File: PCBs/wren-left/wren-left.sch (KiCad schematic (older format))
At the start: 95 parts, among them J1 TRRS_Jack, SW0 Reset, U1 Elite-C

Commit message: Reposition Rotary Encoder and Create New Right Board
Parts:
- added H1, H2, H3, H4, H5, H6, H7: MountingHole, MountingHole:MountingHole_2.2mm_M2_ISO7380, symbol Mechanical:MountingHole
- U1: symbol keebio:Elite-C -> wren-left-rescue:Elite-C-keebio
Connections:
- net COL0: now also MX41.1 (COL); no longer ENC1.S1
- net COL1: now also MX42.1 (COL); no longer MX41.1 (COL)
- net COL2: now also MX43.1 (COL); no longer MX42.1 (COL)
- net COL3: now also MX44.1 (COL); no longer MX43.1 (COL)
- net COL4: now also ENC1.S2; no longer MX44.1 (COL)
- net at MX41.2 (ROW): now also D41.2 (A); no longer D42.2 (A)
- net at MX42.2 (ROW): now also D42.2 (A); no longer D43.2 (A)
- net at MX43.2 (ROW): now also D43.2 (A); no longer D44.2 (A)
- net at MX44.2 (ROW): now also D44.2 (A); no longer D45.2 (A)
- removed net ENC1-OUT: D41.2 (A), ENC1.S2
- new net ENC1-IN: D45.2 (A), ENC1.S1
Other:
- moved on the sheet: ENC1, MX41, MX42, MX43, MX44
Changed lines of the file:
@@
 $EndComp
 $Comp
-L MX_Alps_Hybrid:MX-NoLED MX41
-U 1 1 6072AAD1
+L MX_Alps_Hybrid:MX-NoLED MX42
+U 1 1 6072B58C
 P 5600 5550
-F 0 "MX41" H 5633 5773 60  0000 C CNN
+F 0 "MX42" H 5633 5773 60  0000 C CNN
 F 1 "MX-NoLED" H 5633 5699 20  0000 C CNN
-F 2 "MX_Only:MX-2U-FLIPPED-ReversedStabilizers" H 4975 5525 60  0001 C CNN
+F 2 "MX_Only:MX-1U" H 4975 5525 60  0001 C CNN
 F 3 "" H 4975 5525 60  0001 C CNN
 	1    5600 5550
@@
 $EndComp
 $Comp
-L MX_Alps_Hybrid:MX-NoLED MX42
-U 1 1 6072B58C
+L MX_Alps_Hybrid:MX-NoLED MX43
+U 1 1 6072BC7D
 P 6100 5550
-F 0 "MX42" H 6133 5773 60  0000 C CNN
+F 0 "MX43" H 6133 5773 60  0000 C CNN
 F 1 "MX-NoLED" H 6133 5699 20  0000 C CNN
 F 2 "MX_Only:MX-1U" H 5475 5525 60  0001 C CNN
@@
 $EndComp
 $Comp
-L MX_Alps_Hybrid:MX-NoLED MX43
-U 1 1 6072BC7D
+L MX_Alps_Hybrid:MX-NoLED MX44
+U 1 1 6072C094
 P 6600 5550
-F 0 "MX43" H 6633 5773 60  0000 C CNN
+F 0 "MX44" H 6633 5773 60  0000 C CNN
 F 1 "MX-NoLED" H 6633 5699 20  0000 C CNN
 F 2 "MX_Only:MX-1U" H 5975 5525 60  0001 C CNN
 F 3 "" H 5975 5525 60  0001 C CNN
 	1    6600 5550
-	1    0    0    -1
-$EndComp
-$Comp
-L MX_Alps_Hybrid:MX-NoLED MX44
-U 1 1 6072C094
-P 7100 5550
-F 0 "MX44" H 7133 5773 60  0000 C CNN
-F 1 "MX-NoLED" H 7133 5699 20  0000 C CNN
-F 2 "MX_Only:MX-1U" H 6475 5525 60  0001 C CNN
-F 3 "" H 6475 5525 60  0001 C CNN
-	1    7100 5550
 	1    0    0    -1
 $EndComp
@@
 L Device:Rotary_Encoder_Switch ENC1
 U 1 1 60759DC4
-P 1700 6350
-F 0 "ENC1" H 1700 6717 50  0000 C CNN
-F 1 "Rotary_Encoder_Switch" H 1700 6626 50  0000 C CNN
-F 2 "Rotary_Encoder:RotaryEncoder_Alps_EC11E-Switch_Vertical_H20mm" H 1550 6510 50  0001 C CNN
-F 3 "~" H 1700 6610 50  0001 C CNN
-	1    1700 6350
-	1    0    0    -1
-$EndComp
-Text GLabel 1400 6350 0    50   Input ~ 0
+P 2550 5700
+F 0 "ENC1" H 2550 6067 50  0000 C CNN
+F 1 "Rotary_Encoder_Switch" H 2550 5976 50  0000 C CNN
+F 2 "Rotary_Encoder:RotaryEncoder_Alps_EC11E-Switch_Vertical_H20mm" H 2400 5860 50  0001 C CNN
+F 3 "~" H 2550 5960 50  0001 C CNN
+	1    2550 5700
+	1    0    0    -1
+$EndComp
+Text GLabel 2250 5700 0    50   Input ~ 0
 GND
 Connection ~ 7250 4800
@@
 	5250 4800 5250 5500
 Connection ~ 5250 4800
+Connection ~ 4850 5900
+Wire Wire Line
+	4850 5900 5350 5900
+Text GLabel 2850 5600 2    50   Input ~ 0
+ENC1-IN
+Text GLabel 2850 5800 2    50   Input ~ 0
+ENC1-OUT
+Text GLabel 7050 5700 2    50   Input ~ 0
+ENC1-IN
+Text GLabel 2250 5600 0    50   Input ~ 0
+LEFT
+Text GLabel 2250 5800 0    50   Input ~ 0
+RIGHT
+$Comp
+L wren-left-rescue:Elite-C-keebio U1
+U 1 1 6071F7CA
+P 2500 2000
+F 0 "U1" H 2500 2815 50  0000 C CNN
+F 1 "Elite-C" H 2500 2724 50  0000 C CNN
+F 2 "footprints:Elite-C" H 2450 2100 50  0001 C CNN
+F 3 "" H 2450 2100 50  0001 C CNN
+	1    2500 2000
+	1    0    0    -1
+$EndComp
+Text GLabel 2700 2950 3    50   Input ~ 0
+LEFT
+Text GLabel 2600 2950 3    50   Input ~ 0
+RIGHT
+NoConn ~ 2300 2950
+NoConn ~ 2400 2950
+$Comp
+L MX_Alps_Hybrid:MX-NoLED MX41
+U 1 1 6072AAD1
+P 5100 5550
+F 0 "MX41" H 5133 5773 60  0000 C CNN
+F 1 "MX-NoLED" H 5133 5699 20  0000 C CNN
+F 2 "MX_Only:MX-2U-FLIPPED-ReversedStabilizers" H 4475 5525 60  0001 C CNN
+F 3 "" H 4475 5525 60  0001 C CNN
+	1    5100 5550
+	1    0    0    -1
+$EndComp
 $Comp
 L Device:D_Small D41
@@
 	0    -1   -1   0
 $EndComp
-Connection ~ 4850 5900
-Wire Wire Line
-	4850 5900 5350 5900
-Text GLabel 2000 6250 2    50   Input ~ 0
-ENC1-IN
-Text GLabel 2000 6450 2    50   Input ~ 0
+Text GLabel 7250 5500 0    50   Input ~ 0
 ENC1-OUT
-Text GLabel 4850 5700 0    50   Input ~ 0
-ENC1-OUT
-Text GLabel 5250 5500 0    50   Input ~ 0
-ENC1-IN
-Text GLabel 1400 6250 0    50   Input ~ 0
-LEFT
-Text GLabel 1400 6450 0    50   Input ~ 0
-RIGHT
-$Comp
-L keebio:Elite-C U1
-U 1 1 6071F7CA
-P 2500 2000
-F 0 "U1" H 2500 2815 50  0000 C CNN
-F 1 "Elite-C" H 2500 2724 50  0000 C CNN
-F 2 "footprints:Elite-C" H 2450 2100 50  0001 C CNN
-F 3 "" H 2450 2100 50  0001 C CNN
-	1    2500 2000
-	1    0    0    -1
-$EndComp
-Text GLabel 2700 2950 3    50   Input ~ 0
-LEFT
-Text GLabel 2600 2950 3    50   Input ~ 0
-RIGHT
-NoConn ~ 2300 2950
-NoConn ~ 2400 2950
+$Comp
+L Mechanical:MountingHole H3
+U 1 1 607DC9F0
+P 2500 7000
+F 0 "H3" H 2600 7046 50  0000 L CNN
+F 1 "MountingHole" H 2600 6955 50  0000 L CNN
+F 2 "MountingHole:MountingHole_2.2mm_M2_ISO7380" H 2500 7000 50  0001 C CNN
+F 3 "~" H 2500 7000 50  0001 C CNN
+	1    2500 7000
+	1    0    0    -1
+$EndComp
+$Comp
+L Mechanical:MountingHole H5
+U 1 1 607DDEC1
+P 2500 7200
+F 0 "H5" H 2600 7246 50  0000 L CNN
+F 1 "MountingHole" H 2600 7155 50  0000 L CNN
+F 2 "MountingHole:MountingHole_2.2mm_M2_ISO7380" H 2500 7200 50  0001 C CNN
+F 3 "~" H 2500 7200 50  0001 C CNN
+	1    2500 7200
+	1    0    0    -1
+$EndComp
+$Comp
+L Mechanical:MountingHole H7
+U 1 1 607DE302
+P 2500 7400
+F 0 "H7" H 2600 7446 50  0000 L CNN
+F 1 "MountingHole" H 2600 7355 50  0000 L CNN
+F 2 "MountingHole:MountingHole_2.2mm_M2_ISO7380" H 2500 7400 50  0001 C CNN
+F 3 "~" H 2500 7400 50  0001 C CNN
+	1    2500 7400
+	1    0    0    -1
+$EndComp
+$Comp
+L Mechanical:MountingHole H1
+U 1 1 607DE5EF
+P 2500 6800
+F 0 "H1" H 2600 6846 50  0000 L CNN
+F 1 "MountingHole" H 2600 6755 50  0000 L CNN
+F 2 "MountingHole:MountingHole_2.2mm_M2_ISO7380" H 2500 6800 50  0001 C CNN
+F 3 "~" H 2500 6800 50  0001 C CNN
+	1    2500 6800
+	1    0    0    -1
+$EndComp
+$Comp
+L Mechanical:MountingHole H2
+U 1 1 607DE9D9
+P 3250 6800
+F 0 "H2" H 3350 6846 50  0000 L CNN
+F 1 "MountingHole" H 3350 6755 50  0000 L CNN
+F 2 "MountingHole:MountingHole_2.2mm_M2_ISO7380" H 3250 6800 50  0001 C CNN
+F 3 "~" H 3250 6800 50  0001 C CNN
+	1    3250 6800
+	1    0    0    -1
+$EndComp
+$Comp
+L Mechanical:MountingHole H4
+U 1 1 607DED77
+P 3250 7000
+F 0 "H4" H 3350 7046 50  0000 L CNN
+F 1 "MountingHole" H 3350 6955 50  0000 L CNN
+F 2 "MountingHole:MountingHole_2.2mm_M2_ISO7380" H 3250 7000 50  0001 C CNN
+F 3 "~" H 3250 7000 50  0001 C CNN
+	1    3250 7000
+	1    0    0    -1
+$EndComp
+$Comp
+L Mechanical:MountingHole H6
+U 1 1 607DF460
+P 3250 7200
+F 0 "H6" H 3350 7246 50  0000 L CNN
+F 1 "MountingHole" H 3350 7155 50  0000 L CNN
+F 2 "MountingHole:MountingHole_2.2mm_M2_ISO7380" H 3250 7200 50  0001 C CNN
+F 3 "~" H 3250 7200 50  0001 C CNN
+	1    3250 7200
+	1    0    0    -1
+$EndComp
+Wire Wire Line
+	4850 5700 5050 5700
 $EndSCHEMATC

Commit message: Various Updates
New plates, updated routing on the right side, assorted other changes.
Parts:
- H1, H2, H3, H4, H5, H6, H7: footprint MountingHole:MountingHole_2.2mm_M2_ISO7380 -> MountingHole:MountingHole_5.5mm
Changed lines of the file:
@@
 F 0 "H3" H 2600 7046 50  0000 L CNN
 F 1 "MountingHole" H 2600 6955 50  0000 L CNN
-F 2 "MountingHole:MountingHole_2.2mm_M2_ISO7380" H 2500 7000 50  0001 C CNN
+F 2 "MountingHole:MountingHole_5.5mm" H 2500 7000 50  0001 C CNN
 F 3 "~" H 2500 7000 50  0001 C CNN
 	1    2500 7000
@@
 F 0 "H5" H 2600 7246 50  0000 L CNN
 F 1 "MountingHole" H 2600 7155 50  0000 L CNN
-F 2 "MountingHole:MountingHole_2.2mm_M2_ISO7380" H 2500 7200 50  0001 C CNN
+F 2 "MountingHole:MountingHole_5.5mm" H 2500 7200 50  0001 C CNN
 F 3 "~" H 2500 7200 50  0001 C CNN
 	1    2500 7200
@@
 F 0 "H7" H 2600 7446 50  0000 L CNN
 F 1 "MountingHole" H 2600 7355 50  0000 L CNN
-F 2 "MountingHole:MountingHole_2.2mm_M2_ISO7380" H 2500 7400 50  0001 C CNN
+F 2 "MountingHole:MountingHole_5.5mm" H 2500 7400 50  0001 C CNN
 F 3 "~" H 2500 7400 50  0001 C CNN
 	1    2500 7400
@@
 F 0 "H1" H 2600 6846 50  0000 L CNN
 F 1 "MountingHole" H 2600 6755 50  0000 L CNN
-F 2 "MountingHole:MountingHole_2.2mm_M2_ISO7380" H 2500 6800 50  0001 C CNN
+F 2 "MountingHole:MountingHole_5.5mm" H 2500 6800 50  0001 C CNN
 F 3 "~" H 2500 6800 50  0001 C CNN
 	1    2500 6800
@@
 F 0 "H2" H 3350 6846 50  0000 L CNN
 F 1 "MountingHole" H 3350 6755 50  0000 L CNN
-F 2 "MountingHole:MountingHole_2.2mm_M2_ISO7380" H 3250 6800 50  0001 C CNN
+F 2 "MountingHole:MountingHole_5.5mm" H 3250 6800 50  0001 C CNN
 F 3 "~" H 3250 6800 50  0001 C CNN
 	1    3250 6800
@@
 F 0 "H4" H 3350 7046 50  0000 L CNN
 F 1 "MountingHole" H 3350 6955 50  0000 L CNN
-F 2 "MountingHole:MountingHole_2.2mm_M2_ISO7380" H 3250 7000 50  0001 C CNN
+F 2 "MountingHole:MountingHole_5.5mm" H 3250 7000 50  0001 C CNN
 F 3 "~" H 3250 7000 50  0001 C CNN
 	1    3250 7000
@@
 F 0 "H6" H 3350 7246 50  0000 L CNN
 F 1 "MountingHole" H 3350 7155 50  0000 L CNN
-F 2 "MountingHole:MountingHole_2.2mm_M2_ISO7380" H 3250 7200 50  0001 C CNN
+F 2 "MountingHole:MountingHole_5.5mm" H 3250 7200 50  0001 C CNN
 F 3 "~" H 3250 7200 50  0001 C CNN
 	1    3250 7200

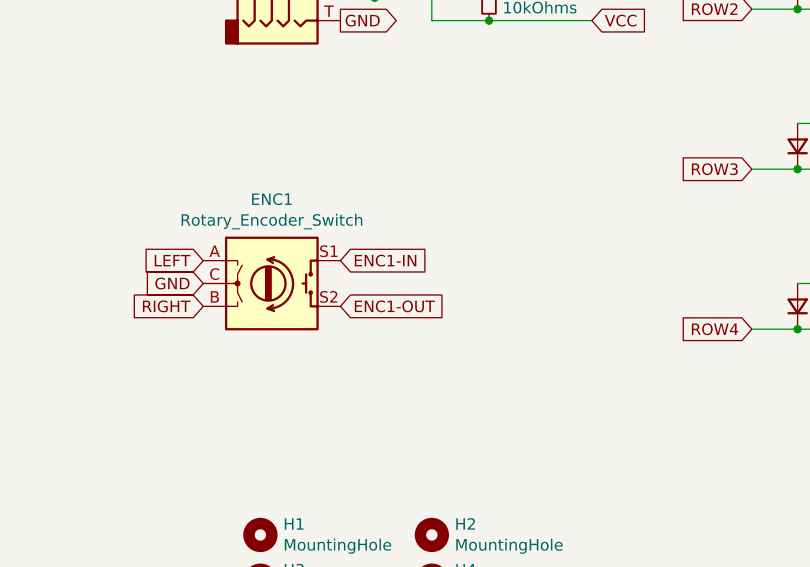
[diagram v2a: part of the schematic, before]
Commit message: Use insight on rotary encoder position to adopt more Kyria-like stagger
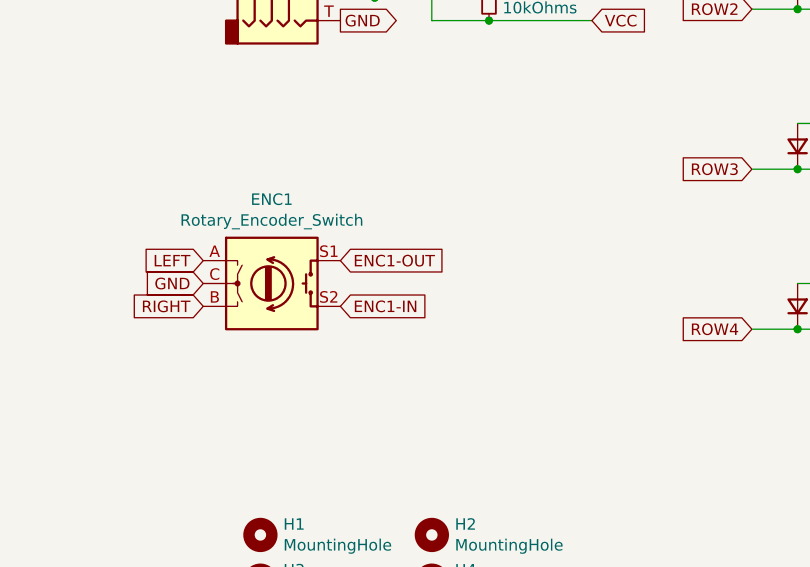
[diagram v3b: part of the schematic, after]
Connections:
- net COL4: now also ENC1.S1; no longer ENC1.S2
- net ENC1-IN: now also ENC1.S2; no longer ENC1.S1
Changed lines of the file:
@@
 Wire Wire Line
 	4850 5900 5350 5900
+Text GLabel 2850 5800 2    50   Input ~ 0
+ENC1-IN
 Text GLabel 2850 5600 2    50   Input ~ 0
-ENC1-IN
-Text GLabel 2850 5800 2    50   Input ~ 0
 ENC1-OUT
 Text GLabel 7050 5700 2    50   Input ~ 0

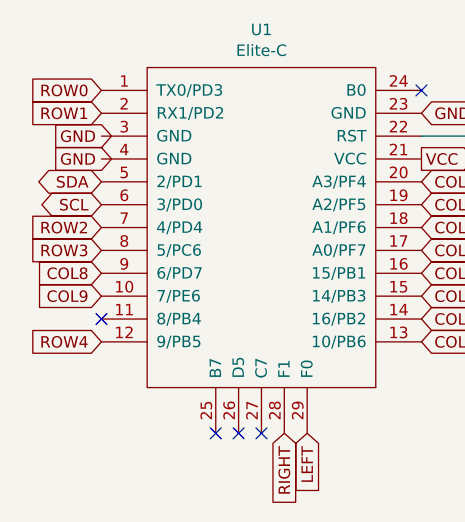
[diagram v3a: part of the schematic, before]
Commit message: Finish left side kyria-like stagger
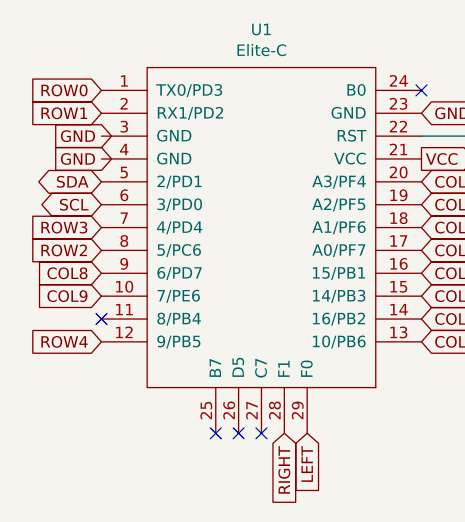
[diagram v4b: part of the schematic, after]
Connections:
- net ROW2: now also U1.8 (5/PC6); no longer U1.7 (4/PD4)
- net ROW3: now also U1.7 (4/PD4); no longer U1.8 (5/PC6)
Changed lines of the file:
@@
 Text GLabel 1800 1550 0    50   Input ~ 0
 ROW1
+Text GLabel 1800 2150 0    50   Input ~ 0
+ROW2
 Text GLabel 1800 2050 0    50   Input ~ 0
-ROW2
-Text GLabel 1800 2150 0    50   Input ~ 0
 ROW3
 Text GLabel 1800 2550 0    50   Input ~ 0

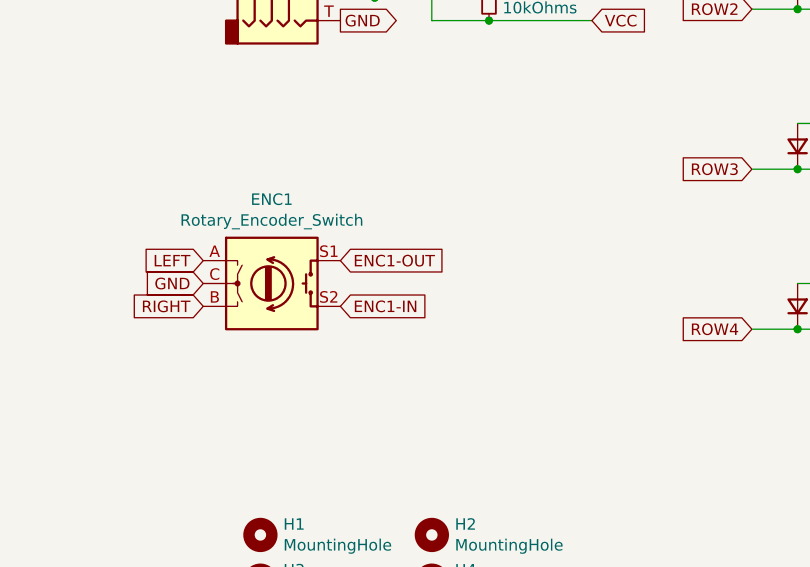
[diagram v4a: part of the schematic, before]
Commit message: Finalize encoder position on left side
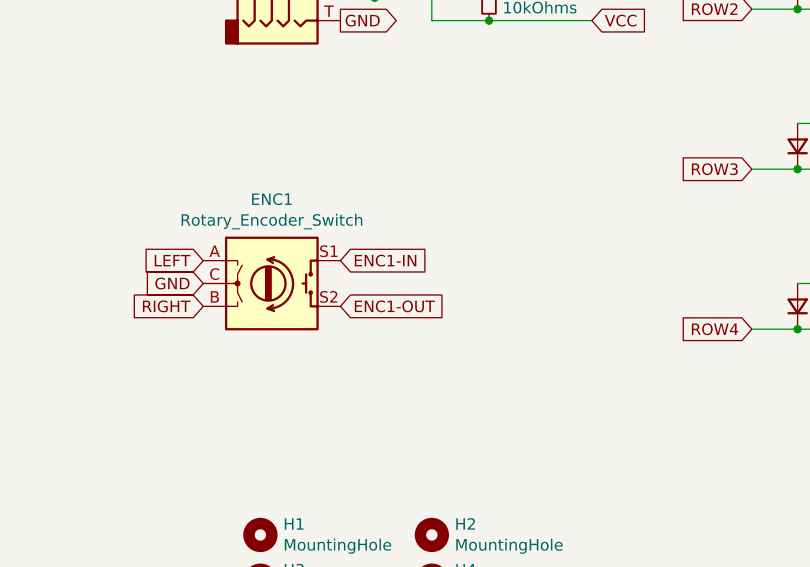
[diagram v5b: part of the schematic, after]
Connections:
- net COL4: now also ENC1.S2; no longer ENC1.S1
- net ENC1-IN: now also ENC1.S1; no longer ENC1.S2
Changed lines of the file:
@@
 Wire Wire Line
 	4850 5900 5350 5900
+Text GLabel 2850 5600 2    50   Input ~ 0
+ENC1-IN
 Text GLabel 2850 5800 2    50   Input ~ 0
-ENC1-IN
-Text GLabel 2850 5600 2    50   Input ~ 0
 ENC1-OUT
 Text GLabel 7050 5700 2    50   Input ~ 0
